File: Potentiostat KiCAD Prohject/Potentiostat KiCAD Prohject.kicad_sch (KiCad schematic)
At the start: 51 parts, among them J1 Conn_01x02_Pin, J2 USB_C_Receptacle_USB2.0, J3 Conn_01x02_Pin, J4 Reference Electrode, J5 Working Electrode, J6 Working Electrode, K1 DIPxx-1Axx-12xD, SW1 Reset, SW2 Boot, U1 OPA2277, U10 ADS1115IDGS, U11 MCP4725xxx-xCH, U13 LD1117S33TR_SOT223, U14 ESP32-S2-SOLO, U2 TL074, U4 OPA2277, U5 INA128, U6 MCP4725xxx-xCH, U7 INA128, U8 REF3033, U9 INA128

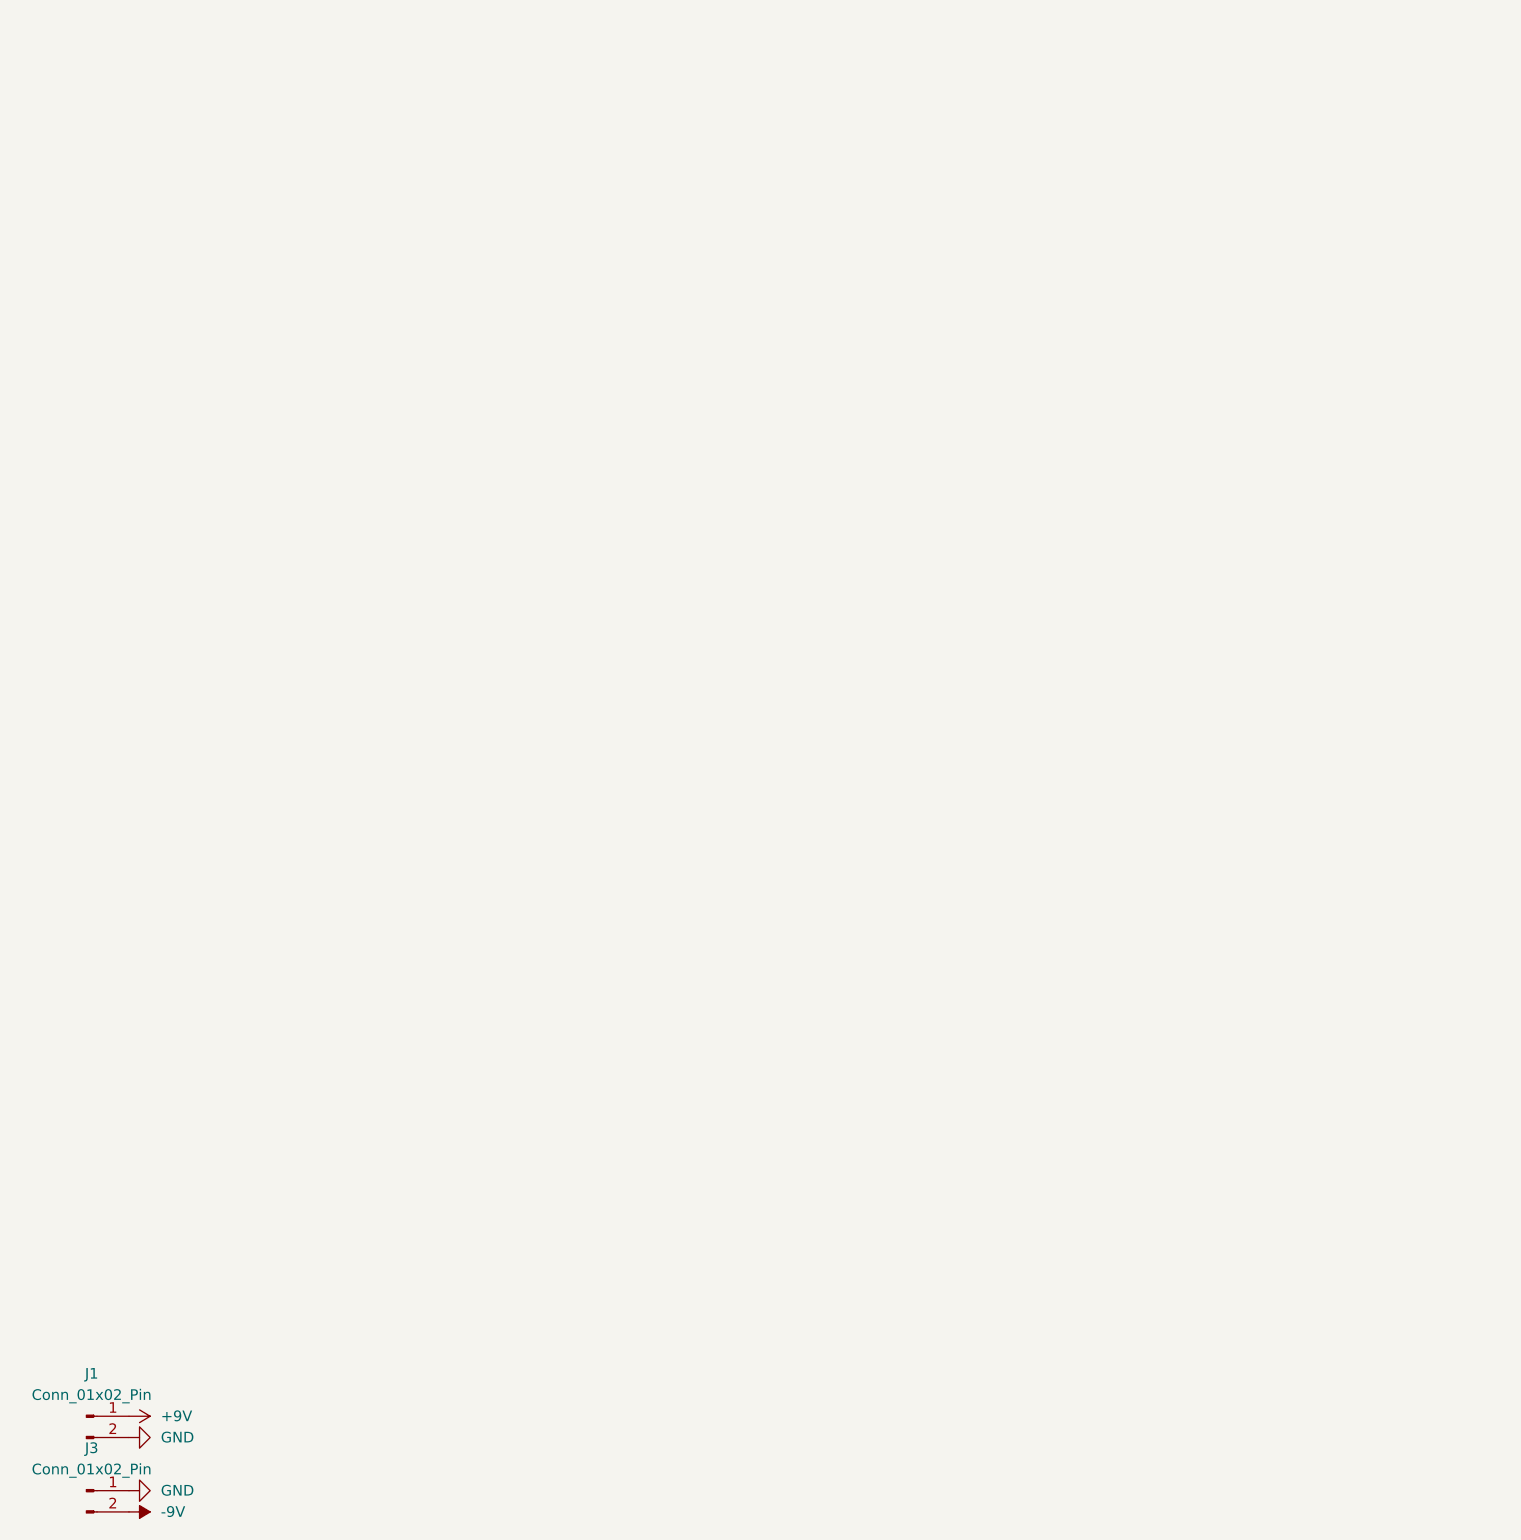
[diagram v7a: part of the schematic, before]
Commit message: almost finished layout -- need test points
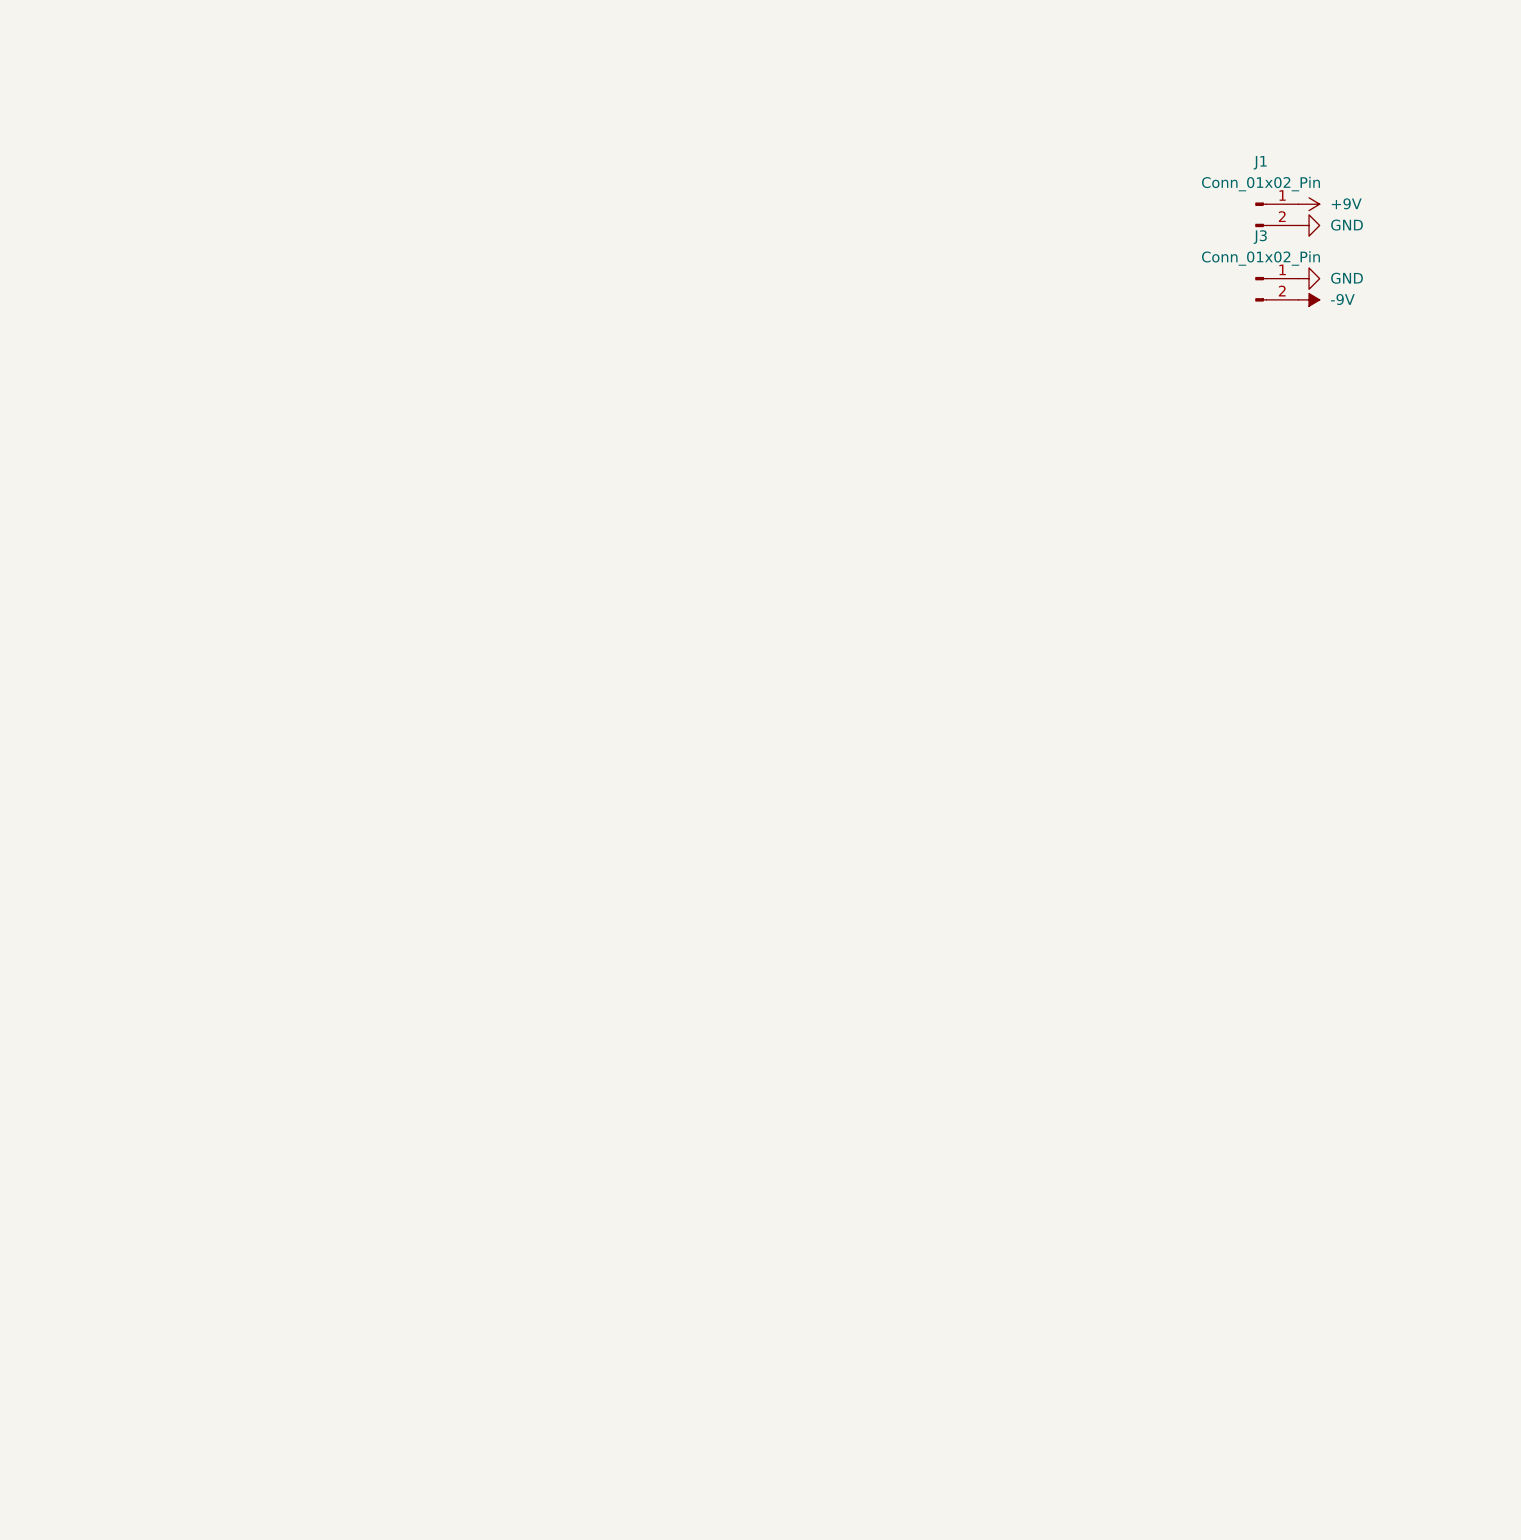
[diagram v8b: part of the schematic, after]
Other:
- moved on the sheet: J1, J3
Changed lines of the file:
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@@
 	(symbol
 		(lib_id "Connector:Conn_01x02_Pin")
-		(at 20.32 397.51 0)
+		(at 160.02 252.73 0)
 		(unit 1)
 		(exclude_from_sim no)
@@
 		(fields_autoplaced yes)
 		(property "Reference" "J3"
-			(at 20.955 392.43 0)
+			(at 160.655 247.65 0)
 			(effects
 				(font
@@
 		)
 		(property "Value" "Conn_01x02_Pin"
-			(at 20.955 394.97 0)
+			(at 160.655 250.19 0)
 			(effects
 				(font
@@
 		)
 		(property "Footprint" "Connector_PinHeader_2.54mm:PinHeader_1x02_P2.54mm_Vertical"
-			(at 20.32 397.51 0)
+			(at 160.02 252.73 0)
 			(effects
 				(font
@@
 		)
 		(property "Datasheet" "~"
-			(at 20.32 397.51 0)
+			(at 160.02 252.73 0)
 			(effects
 				(font
@@
 		)
 		(property "Description" "Generic connector, single row, 01x02, script generated"
-			(at 20.32 397.51 0)
+			(at 160.02 252.73 0)
 			(effects
 				(font
@@
 	(symbol
 		(lib_id "Connector:Conn_01x02_Pin")
-		(at 20.32 388.62 0)
+		(at 160.02 243.84 0)
 		(unit 1)
 		(exclude_from_sim no)
@@
 		(fields_autoplaced yes)
 		(property "Reference" "J1"
-			(at 20.955 383.54 0)
+			(at 160.655 238.76 0)
 			(effects
 				(font
@@
 		)
 		(property "Value" "Conn_01x02_Pin"
-			(at 20.955 386.08 0)
+			(at 160.655 241.3 0)
 			(effects
 				(font
@@
 		)
 		(property "Footprint" "Connector_PinHeader_2.54mm:PinHeader_1x02_P2.54mm_Vertical"
-			(at 20.32 388.62 0)
+			(at 160.02 243.84 0)
 			(effects
 				(font
@@
 		)
 		(property "Datasheet" "~"
-			(at 20.32 388.62 0)
+			(at 160.02 243.84 0)
 			(effects
 				(font
@@
 		)
 		(property "Description" "Generic connector, single row, 01x02, script generated"
-			(at 20.32 388.62 0)
+			(at 160.02 243.84 0)
 			(effects
 				(font
@@
 	(symbol
 		(lib_id "power:+9V")
-		(at 25.4 388.62 270)
+		(at 165.1 243.84 270)
 		(unit 1)
 		(exclude_from_sim no)
@@
 		(fields_autoplaced yes)
 		(property "Reference" "#PWR029"
-			(at 21.59 388.62 0)
+			(at 161.29 243.84 0)
 			(effects
 				(font
@@
 		)
 		(property "Value" "+9V"
-			(at 29.21 388.6199 90)
+			(at 168.91 243.8399 90)
 			(effects
 				(font
@@
 		)
 		(property "Footprint" ""
-			(at 25.4 388.62 0)
+			(at 165.1 243.84 0)
 			(effects
 				(font
@@
 		)
 		(property "Datasheet" ""
-			(at 25.4 388.62 0)
+			(at 165.1 243.84 0)
 			(effects
 				(font
@@
 		)
 		(property "Description" "Power symbol creates a global label with name \"+9V\""
-			(at 25.4 388.62 0)
+			(at 165.1 243.84 0)
 			(effects
 				(font
@@
 	(symbol
 		(lib_id "power:GND")
-		(at 25.4 397.51 90)
+		(at 165.1 252.73 90)
 		(unit 1)
 		(exclude_from_sim no)
@@
 		(fields_autoplaced yes)
 		(property "Reference" "#PWR047"
-			(at 31.75 397.51 0)
+			(at 171.45 252.73 0)
 			(effects
 				(font
@@
 		)
 		(property "Value" "GND"
-			(at 29.21 397.5099 90)
+			(at 168.91 252.7299 90)
 			(effects
 				(font
@@
 		)
 		(property "Footprint" ""
-			(at 25.4 397.51 0)
+			(at 165.1 252.73 0)
 			(effects
 				(font
@@
 		)
 		(property "Datasheet" ""
-			(at 25.4 397.51 0)
+			(at 165.1 252.73 0)
 			(effects
 				(font
@@
 		)
 		(property "Description" "Power symbol creates a global label with name \"GND\" , ground"
-			(at 25.4 397.51 0)
+			(at 165.1 252.73 0)
 			(effects
 				(font
@@
 	(symbol
 		(lib_id "power:-9V")
-		(at 25.4 400.05 270)
+		(at 165.1 255.27 270)
 		(unit 1)
 		(exclude_from_sim no)
@@
 		(fields_autoplaced yes)
 		(property "Reference" "#PWR030"
-			(at 21.59 400.05 0)
+			(at 161.29 255.27 0)
 			(effects
 				(font
@@
 		)
 		(property "Value" "-9V"
-			(at 29.21 400.0499 90)
+			(at 168.91 255.2699 90)
 			(effects
 				(font
@@
 		)
 		(property "Footprint" ""
-			(at 25.4 400.05 0)
+			(at 165.1 255.27 0)
 			(effects
 				(font
@@
 		)
 		(property "Datasheet" ""
-			(at 25.4 400.05 0)
+			(at 165.1 255.27 0)
 			(effects
 				(font
@@
 		)
 		(property "Description" "Power symbol creates a global label with name \"-9V\""
-			(at 25.4 400.05 0)
+			(at 165.1 255.27 0)
 			(effects
 				(font
@@
 	(symbol
 		(lib_id "power:GND")
-		(at 25.4 391.16 90)
+		(at 165.1 246.38 90)
 		(unit 1)
 		(exclude_from_sim no)
@@
 		(fields_autoplaced yes)
 		(property "Reference" "#PWR046"
-			(at 31.75 391.16 0)
+			(at 171.45 246.38 0)
 			(effects
 				(font
@@
 		)
 		(property "Value" "GND"
-			(at 29.21 391.1599 90)
+			(at 168.91 246.3799 90)
 			(effects
 				(font
@@
 		)
 		(property "Footprint" ""
-			(at 25.4 391.16 0)
+			(at 165.1 246.38 0)
 			(effects
 				(font
@@
 		)
 		(property "Datasheet" ""
-			(at 25.4 391.16 0)
+			(at 165.1 246.38 0)
 			(effects
 				(font
@@
 		)
 		(property "Description" "Power symbol creates a global label with name \"GND\" , ground"
-			(at 25.4 391.16 0)
+			(at 165.1 246.38 0)
 			(effects
 				(font
